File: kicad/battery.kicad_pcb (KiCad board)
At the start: 2 copper layers, 13 x 7.9 mm, 1 part

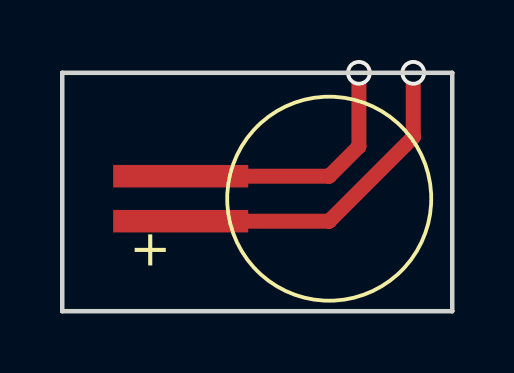
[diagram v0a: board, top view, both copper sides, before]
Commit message: ran drc on hmi2 (is good, no resubmit necessary); slightly moved battery on battery, drc on battery is fine (resubmit though)
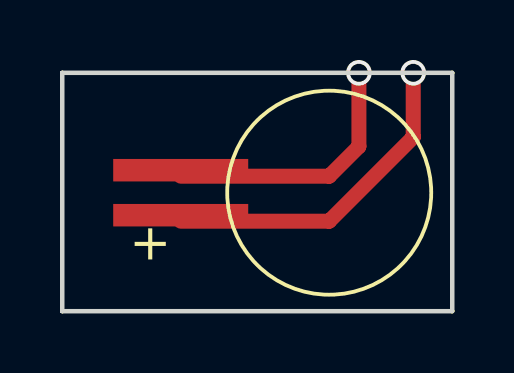
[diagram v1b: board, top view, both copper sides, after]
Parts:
- moved U$5 0.20 mm to (151.5, 111.3)
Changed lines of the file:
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@@
   )
   (module ringRemote:ML621S (layer Top)
-    (at 151.5 111.5 270)
+    (at 151.5 111.3 270)
     (fp_text reference U$5 (at 0 0 270) (layer F.SilkS) hide
       (effects (font (size 1.27 1.27) (thickness 0.15)))
